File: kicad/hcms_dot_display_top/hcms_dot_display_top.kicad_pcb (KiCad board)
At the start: 4 copper layers, 35.5 x 39.9 mm, 56 parts, among them J1 Conn_01x12, J2 USB_C_Receptacle_USB2.0, J3 Conn_01x12, J4 Conn_01x11_Female, J5 Conn_01x11_Male, J6 Conn_01x12, J7 Conn_01x12, J8 Conn_01x02_Male, Q1 Q_PMOS_DSG, Q2 Q_PMOS_DSG, Q3 Q_PMOS_DSG, Q4 Q_PMOS_DSG, Q5 Q_PMOS_DSG, Q6 Q_PMOS_DSG, SW1 SW_DIP_x03, U1 ATtiny1626-X, U2 FT231XS

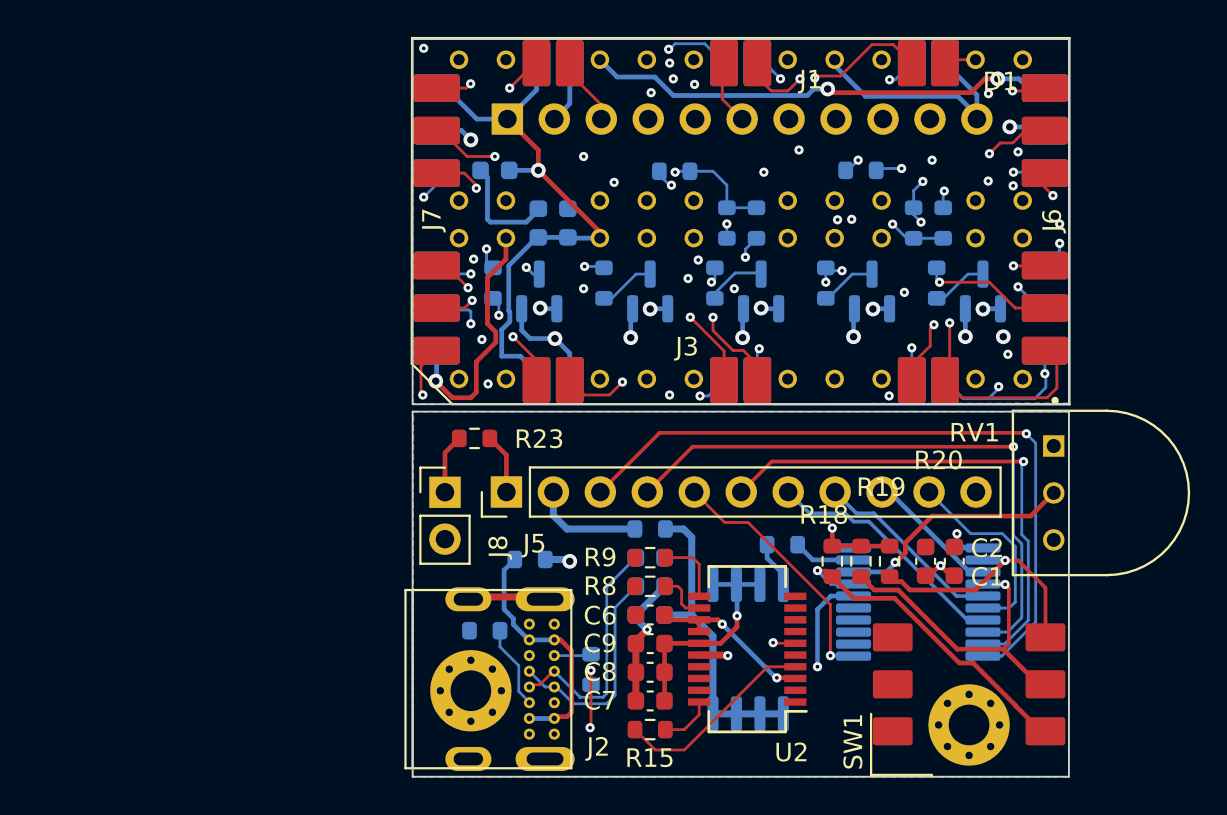
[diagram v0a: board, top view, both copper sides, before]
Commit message: Top board refined
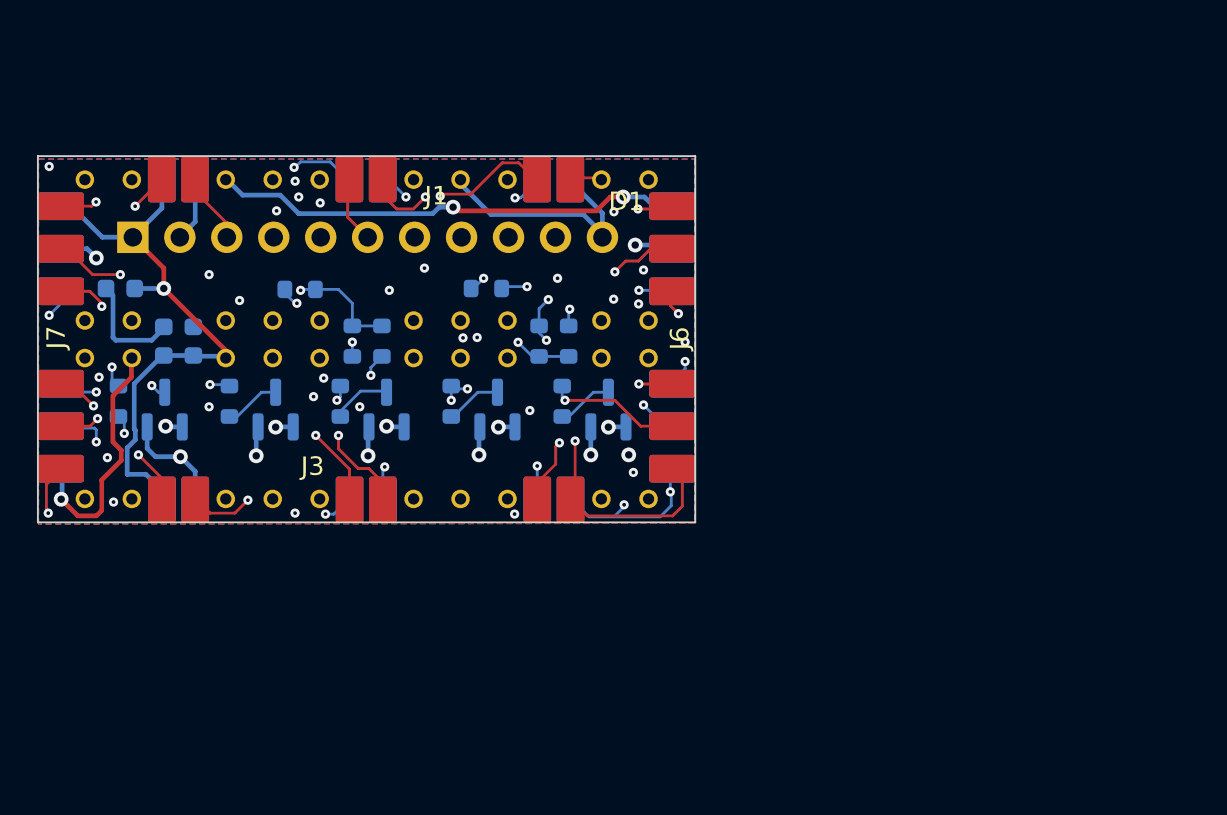
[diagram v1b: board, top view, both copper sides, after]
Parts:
- removed C1, C9: 10nF, Capacitor_SMD:C_0603_1608Metric
- removed C12, C2, C6, C8: 100nF, Capacitor_SMD:C_0603_1608Metric
- removed C4, C5: 47pF, Capacitor_SMD:C_0603_1608Metric
- removed C7: 4.7uF, Capacitor_SMD:C_0603_1608Metric
- removed J2: USB_C_Receptacle_USB2.0, hcms:213716-0001
- removed J5: Conn_01x11_Male, Connector_PinHeader_2.54mm:PinHeader_1x11_P2.54mm_Vertical
- removed J8: Conn_01x02_Male, Connector_PinHeader_2.54mm:PinHeader_1x02_P2.54mm_Vertical
- removed MH1, MH2: MountingHole, MountingHole:MountingHole_2.2mm_M2_Pad_Via
- removed Q6: Q_PMOS_DSG, Package_SO:SO-8_5.3x6.2mm_P1.27mm
- removed R15: 1k, Resistor_SMD:R_0603_1608Metric
- removed R18, R19, R20: 10k, Resistor_SMD:R_0603_1608Metric
- removed R21, R22, R23: 0, Resistor_SMD:R_0603_1608Metric
- removed R3: 200, Resistor_SMD:R_0603_1608Metric
- removed R4, R5: 5.1k, Resistor_SMD:R_0603_1608Metric
- removed R8, R9: 27, Resistor_SMD:R_0603_1608Metric
- removed RV1: R_Potentiometer, hcms:TRIM_3352T-1-201LF
- removed SW1: SW_DIP_x03, hcms:BPA03SB
- removed U1: ATtiny1626-X, Package_SO:SSOP-20_5.3x7.2mm_P0.65mm
- removed U2: FT231XS, Package_SO:SSOP-20_3.9x8.7mm_P0.635mm
- J4: value Conn_01x11_Female -> Conn_01x11_Male; footprint Connector_PinSocket_2.54mm:PinSocket_1x11_P2.54mm_Vertical -> Connector_PinHeader_2.54mm:PinHeader_1x11_P2.54mm_Vertical
- moved J7 21.3 mm to (143.7, 106.0)
- moved J3 21.3 mm to (160.2, 114.8)
- moved D1 21.3 mm to (160.3, 106.1)
- moved C11 21.2 mm to (150.9, 106.2)
- moved C3 21.2 mm to (149.3, 106.2)
- moved R17 21.2 mm to (156.7, 103.4)
- moved C10 21.2 mm to (146.9, 103.3)
- moved Q1 21.2 mm to (161.3, 109.9)
- moved Q2 21.2 mm to (149.3, 109.9)
- moved Q3 21.2 mm to (167.3, 109.9)
- moved Q4 21.2 mm to (155.3, 109.9)
- moved Q5 21.2 mm to (173.3, 109.9)
- moved R1 21.2 mm to (171.2, 106.2)
- moved R10 21.2 mm to (158.8, 109.4)
- moved R11 21.2 mm to (146.8, 109.4)
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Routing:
- net /MCU_COL_2: track 108.1 -> 69.7 mm, vias 8 -> 7
- net /MCU_COL_4: track 103.4 -> 71.0 mm, vias 10 -> 9
- net /MCU_COL_3: track 95.7 -> 68.1 mm, vias 10 -> 9
- net GND: track 66.1 -> 41.8 mm, vias 10 -> 3
- net +5V: track 83.0 -> 63.6 mm, vias 6 -> 3
- net /CONFIG_0: track 18.2 -> 0.00 mm, vias 1 -> 0
- net /CONFIG_1: track 17.0 -> 0.00 mm, vias 1 -> 0
- net Net-(C12-Pad1): track 16.9 -> 0.00 mm
- net /UPDI: track 16.9 -> 0.00 mm, vias 1 -> 0
- net /MCU_COL_5: track 81.2 -> 67.3 mm
- net /MCU_COL_1: track 85.7 -> 71.8 mm, vias 8 -> 7
- net /CONFIG_2: track 13.6 -> 0.00 mm, vias 1 -> 0
- net Net-(J2-PadA4): track 13.6 -> 0.00 mm
- net /D+: track 13.4 -> 0.00 mm
- net /POT: track 12.4 -> 0.00 mm, vias 1 -> 0
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- removed copper zone on F.Cu, net +5V
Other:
- board size 35.5 x 39.9 mm -> 35.6 x 19.8 mm
- board text removed: "ap nl 0422"
- board text removed: "dot display"
- board text removed: "rev 1"

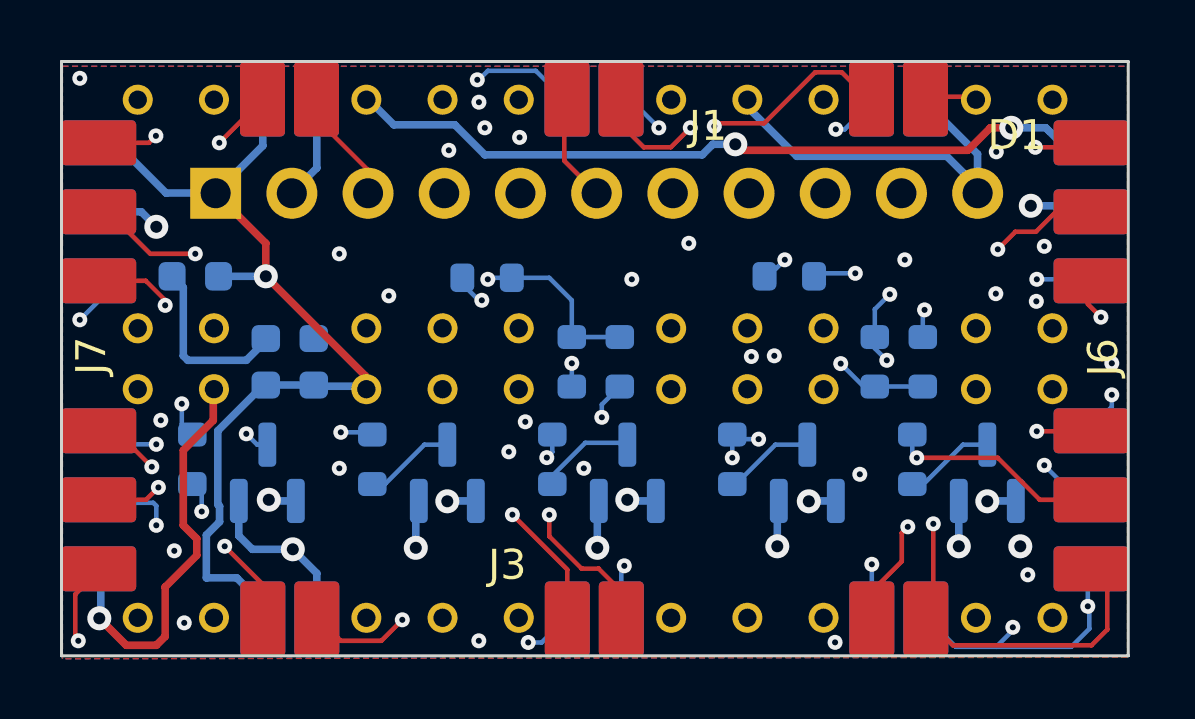
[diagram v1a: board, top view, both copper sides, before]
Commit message: Updated DRCs and fixed connector edge clearance
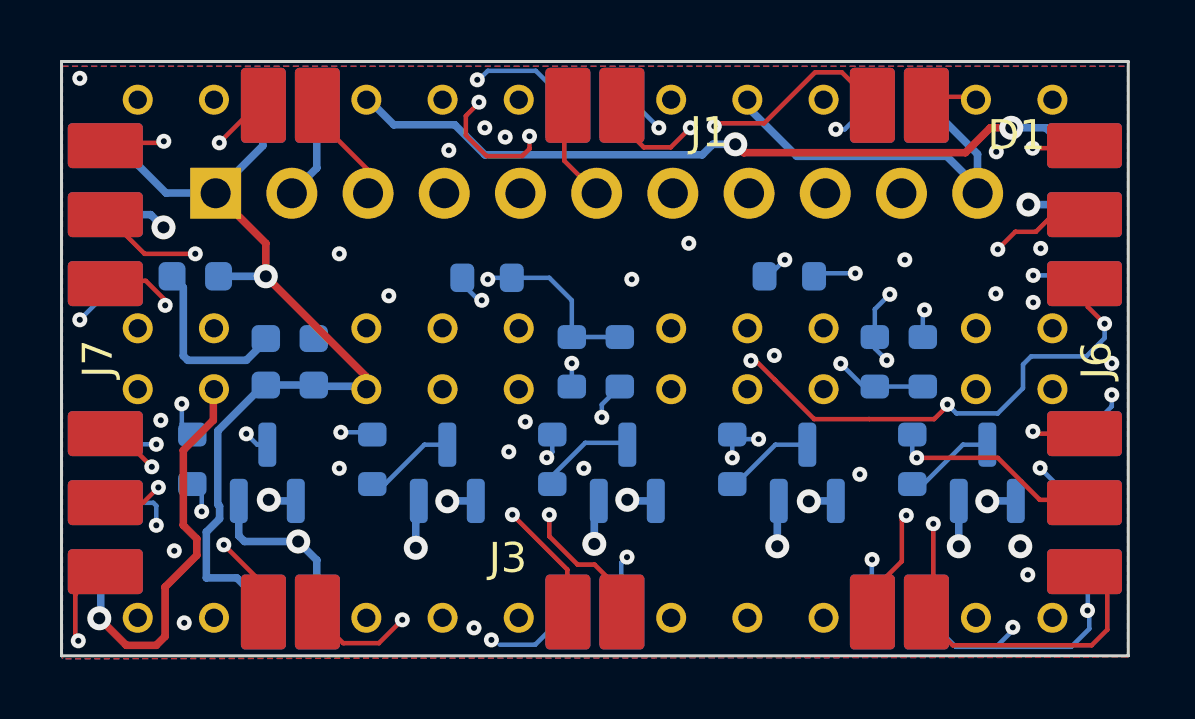
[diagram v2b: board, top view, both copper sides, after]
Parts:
- moved J6 0.24 mm to (176.6, 106.1)
- moved J7 0.24 mm to (143.9, 106.1)
- moved J3 0.23 mm to (160.3, 114.5)
- moved J1 0.21 mm to (160.3, 97.6)
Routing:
- net /CLK: track 81.8 -> 84.1 mm, vias 7 -> 6
- net /MCU_COL_3: track 68.1 -> 70.4 mm, vias 9 -> 10
- net /MCU_COL_4: track 71.0 -> 72.9 mm, vias 9 -> 10
- net /MCU_COL_2: track 69.7 -> 70.8 mm
- net /nBLNK: track 87.9 -> 87.1 mm

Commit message: easter eggs, actually ready for final review. boards passing DRC
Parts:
- added G***: LOGO, LOGO, B.Cu at (163.7, 109.0)
- added G***: LOGO, LOGO, B.Cu at (164.6, 113.2)
